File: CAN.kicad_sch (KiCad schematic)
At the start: 7 parts, among them U12 SIT1051TK/3, U13 ZX-SH1.0-4PWT

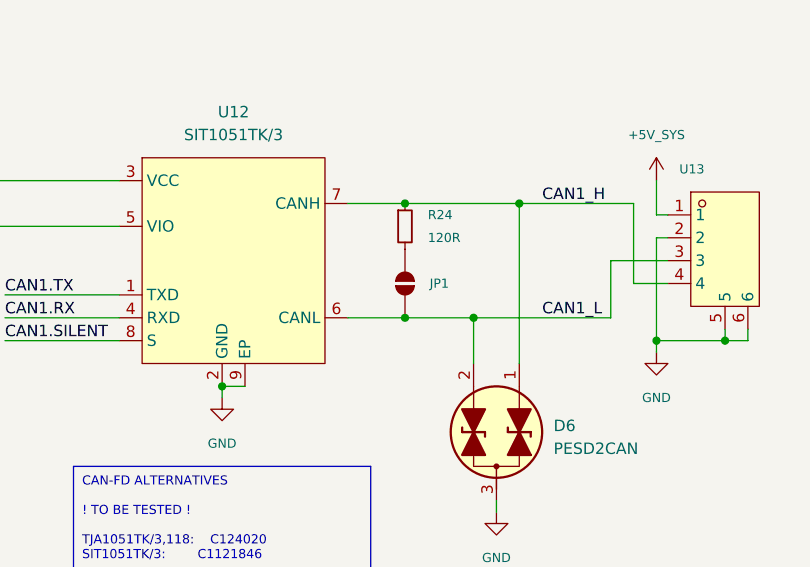
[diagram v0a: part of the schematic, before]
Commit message: BOM LCSC numbers assigned
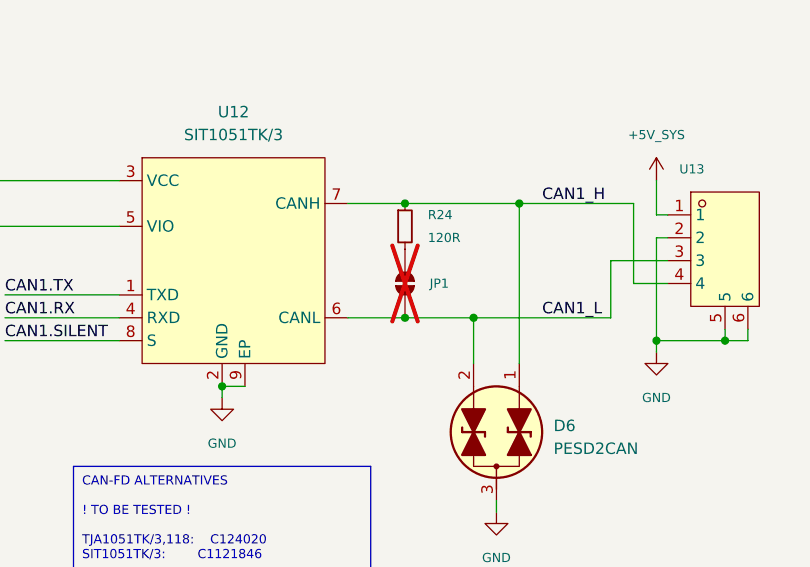
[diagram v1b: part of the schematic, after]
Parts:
- C39, C40: LCSC Part (none) -> C1525
- JP1: now not fitted
- R24: LCSC Part (none) -> C25079
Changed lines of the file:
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@@
+			)
+		)
+		(property "LCSC Part" "C1525"
+			(at 69.85 66.04 0)
+			(hide yes)
+			(show_name no)
+			(do_not_autoplace no)
+			(effects
+				(font
+					(size 1.27 1.27)
+				)
 			)
 		)
@@
 		(exclude_from_sim no)
 		(in_bom no)
-		(on_board yes)
-		(in_pos_files yes)
-		(dnp no)
+		(on_board no)
+		(in_pos_files yes)
+		(dnp yes)
 		(property "Reference" "JP1"
 			(at 124.46 68.58 90)
@@
 			)
 		)
+		(property "LCSC Part" "C1525"
+			(at 64.77 66.04 0)
+			(hide yes)
+			(show_name no)
+			(do_not_autoplace no)
+			(effects
+				(font
+					(size 1.27 1.27)
+				)
+			)
+		)
 		(pin "1"
 		)
@@
 			(at 120.65 62.23 0)
 			(hide yes)
+			(show_name no)
+			(do_not_autoplace no)
+			(effects
+				(font
+					(size 1.27 1.27)
+				)
+			)
+		)
+		(property "LCSC Part" "C25079"
+			(at 120.65 62.23 0)
+			(hide yes)
